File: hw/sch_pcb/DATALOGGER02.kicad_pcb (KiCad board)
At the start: 2 copper layers, 101.1 x 60.5 mm, 161 parts, among them IC1 CY15B108QN-40SXI, IC2 FM3164-G, IC3 LTC4041EUFD#PBF, J1 HEADER_2x01_PARALLEL, J10 HEADER_2x05_PARALLEL, J11 HEADER_2x07_PARALLEL, J12 HEADER_2x05_PARALLEL, J13 HEADER_2x02_PARALLEL, J14 Conn_01x06_Female, J2 HEADER_2x01, J23 MCX, J24 HEADER_2x03_PARALLEL, J3 HEADER_2x03, J4 HEADER_2x03_PARALLEL, J5 HEADER_2x03_PARALLEL, J6 MCC-SD (kouka z modulu), J7 Conn_01x06_Female, J8 Conn_01x07_Female, J9 Conn_01x04_Female, Q1 DMP2045UQ-7, Q2 DMTH3002LPS, Q3 DMTH3002LPS, U1 ISL21080CIH320Z-TK, U10 TPS631000DRLR, U11 SX1262, U12 PE4259, U2 LM4041CIM3-1.2(neosazovat), U3 ATMEGA1284P-AU, U4 TXS0108EPW, U5 ICM-20948, U6 TPS22965-Q1, U7 MS5611-01BA, U8 MIC5504-1.8YM5-TR, U9 TPS631000DRLR, Y2 6pF crystal - 32.768kHz, Y3 32MHz, Y6 8MHz LFXTAL083138

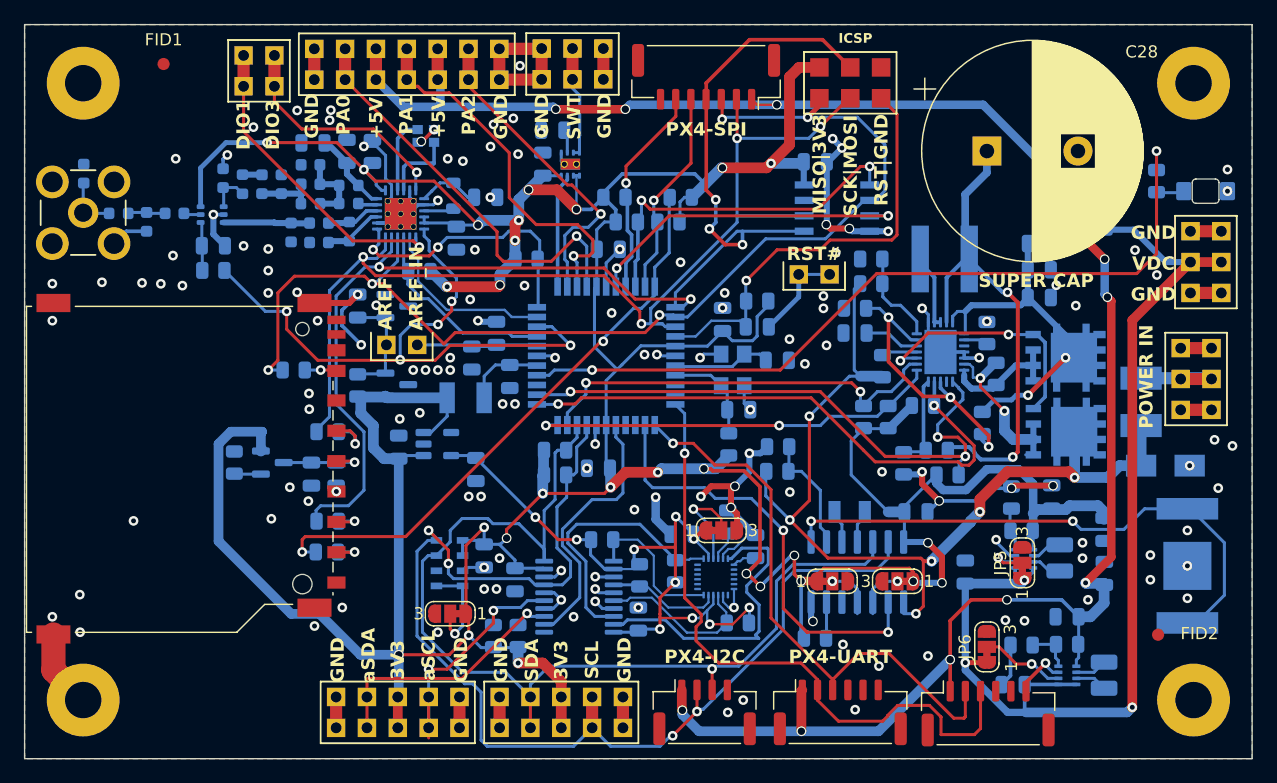
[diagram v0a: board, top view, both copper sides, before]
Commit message: track width changes
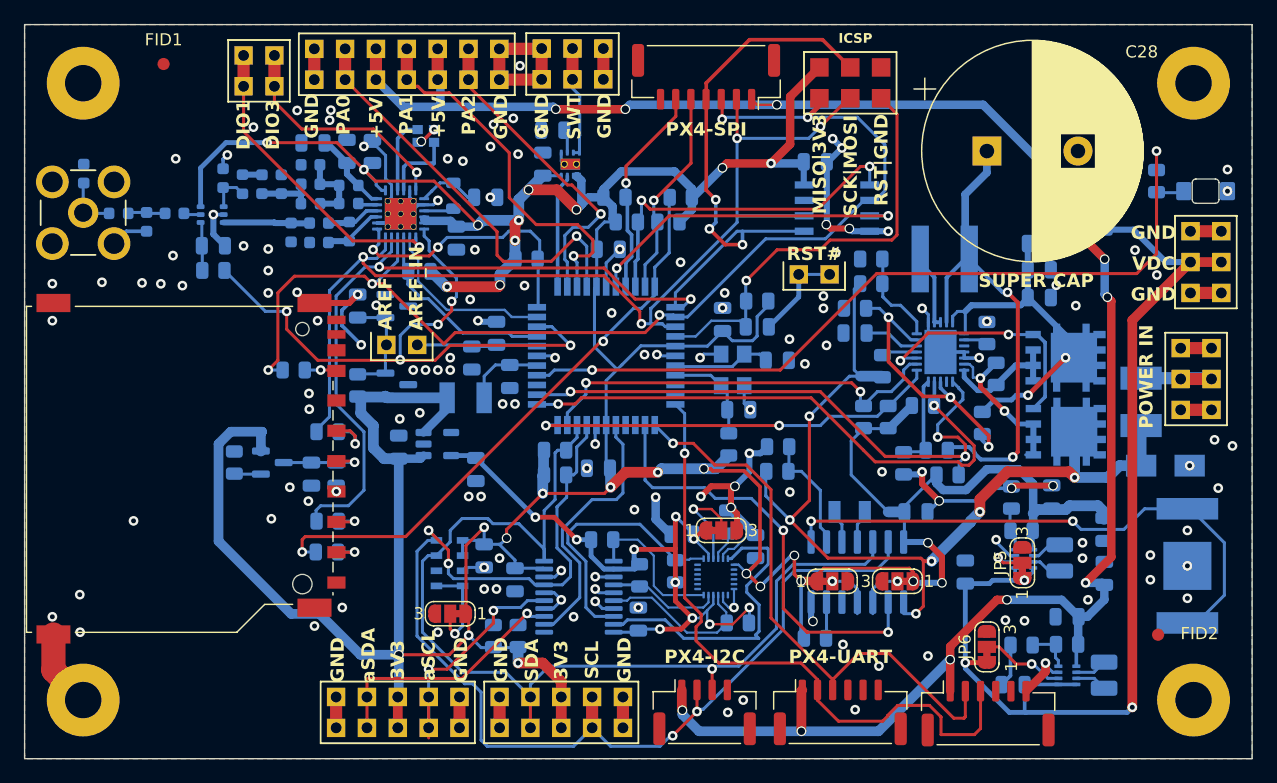
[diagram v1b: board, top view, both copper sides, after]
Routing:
- net Net-(IC3-VIN): track 15.4 -> 13.4 mm
- net +3.3V: track 383.5 -> 381.7 mm
- net +5V: track 162.9 -> 162.1 mm

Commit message: track width changes
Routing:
- net GND: track 180.8 -> 179.4 mm, vias 141 -> 142

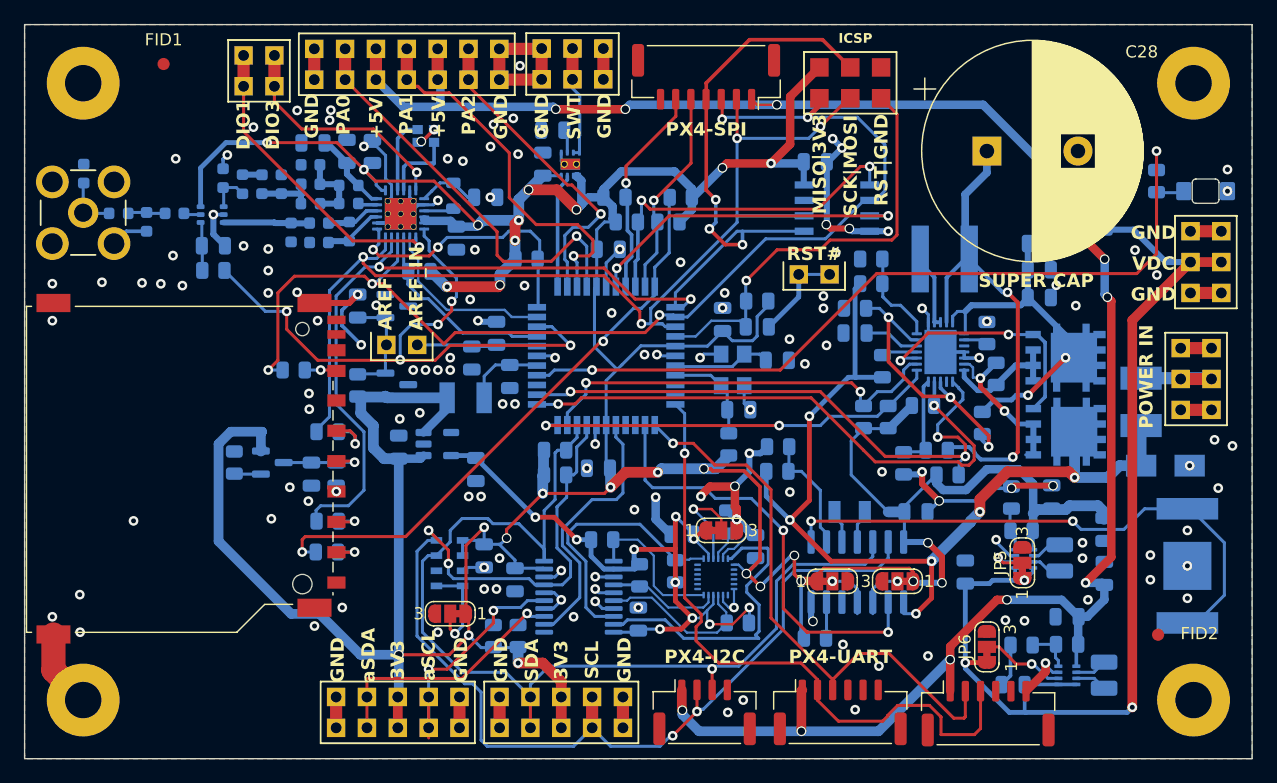
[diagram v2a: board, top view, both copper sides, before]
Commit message: Update footprints. Run DRC check.
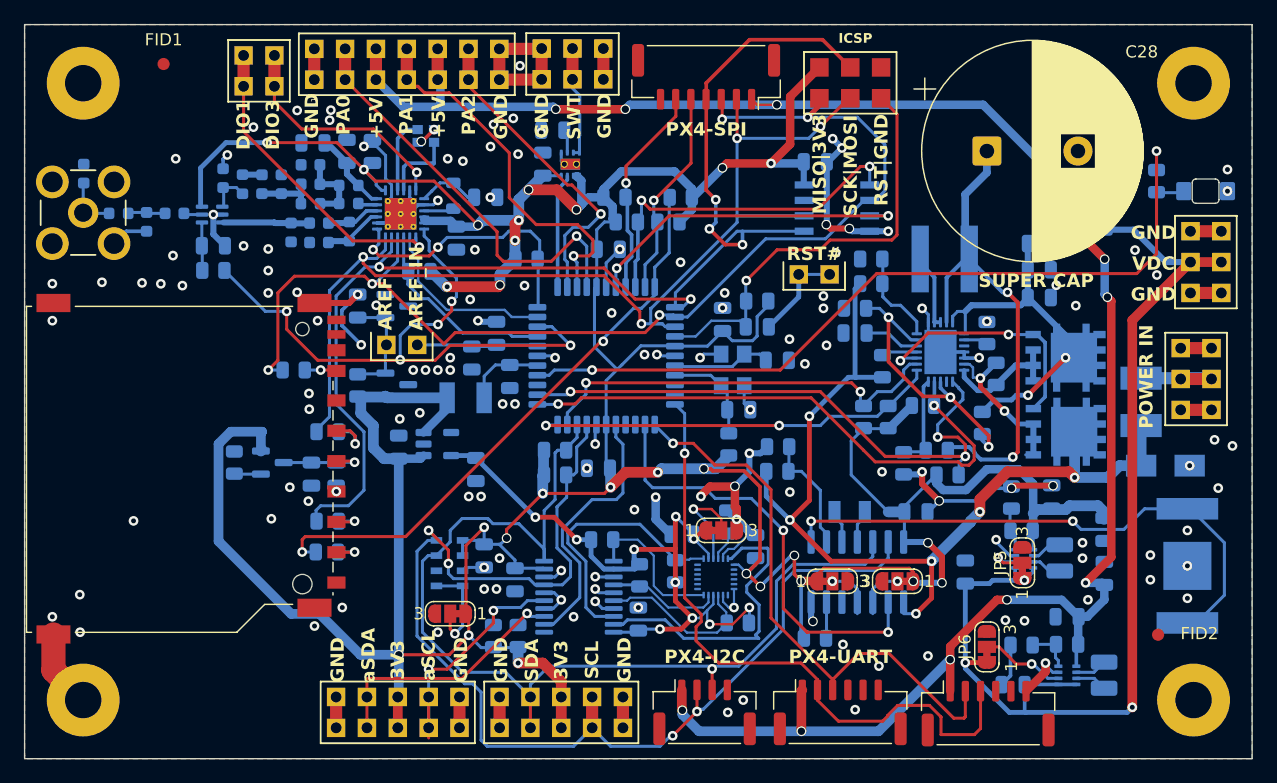
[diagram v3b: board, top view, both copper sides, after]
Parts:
- J23: value MCX -> VAL**
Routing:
- net GND: vias 142 -> 141
